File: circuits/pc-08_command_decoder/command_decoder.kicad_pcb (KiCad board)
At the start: 2 copper layers, 99.1 x 99.1 mm, 17 parts, among them U1 74HC138, U2 74HC138, U3 74HC138, U4 74HC138, U5 4011, U6 4011, U7 74HC138, U8 4011

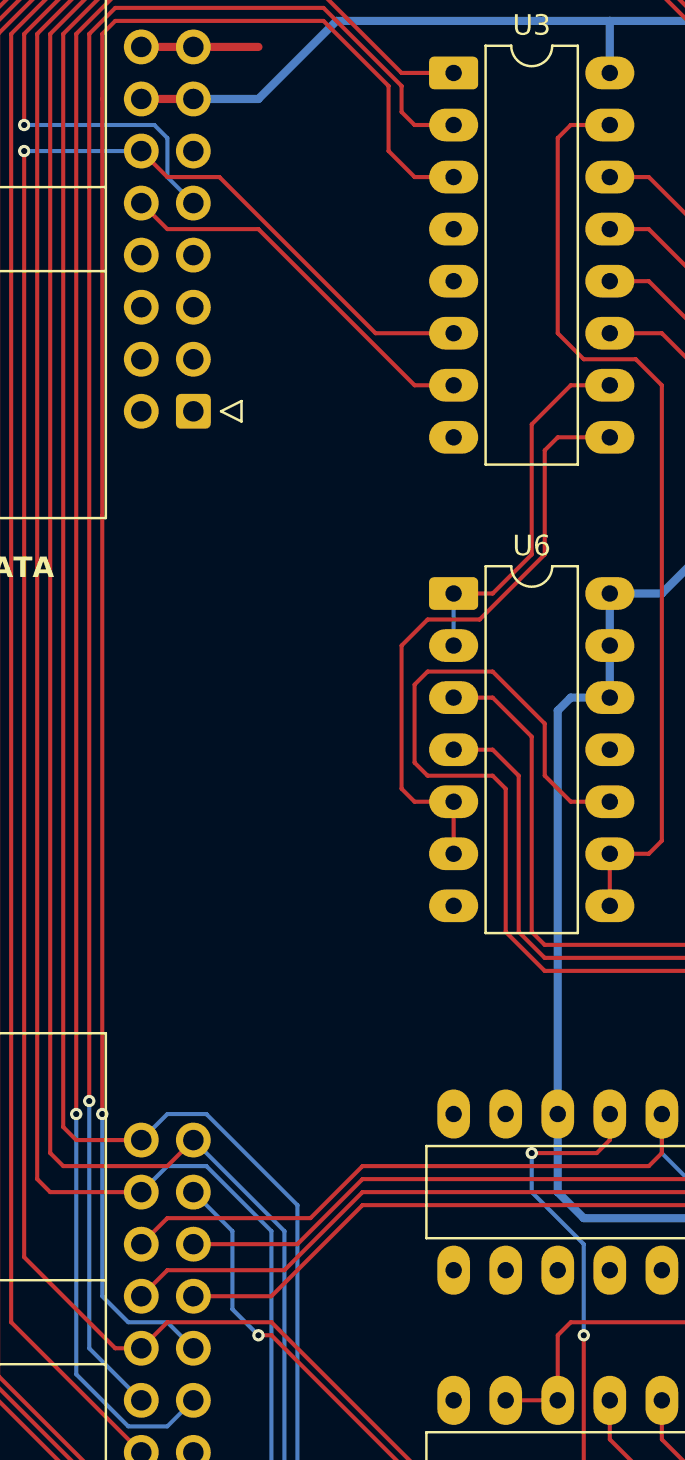
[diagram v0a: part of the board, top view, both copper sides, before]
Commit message: add pull-up resistor network to command decoder
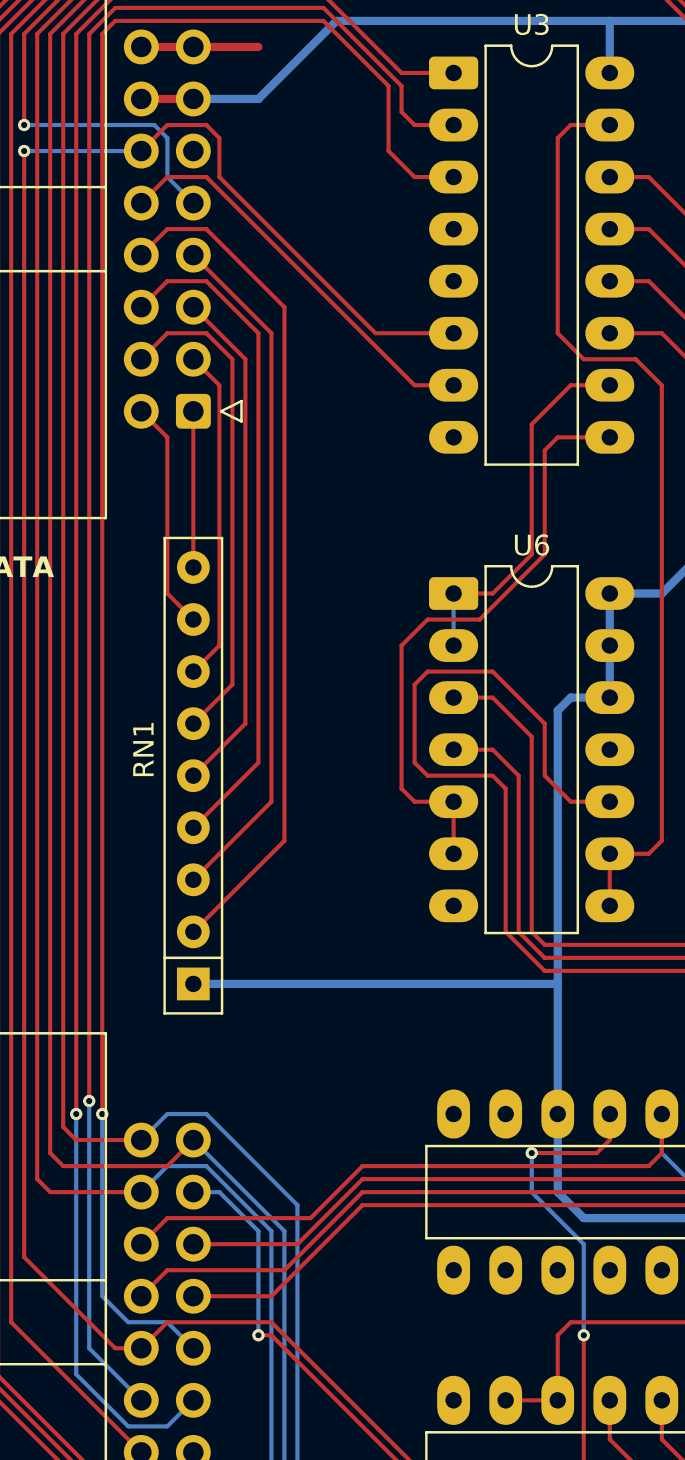
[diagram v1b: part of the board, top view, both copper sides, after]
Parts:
- added RN1: R_Network08, Resistor_THT:R_Array_SIP9, F.Cu at (54.6, 82.5)
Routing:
- net /data7: track 0.00 -> 41.4 mm
- net /data6: track 0.00 -> 33.6 mm
- net /data5: track 0.00 -> 32.7 mm
- net /data4: track 0.00 -> 25.0 mm
- net /data3: track 0.00 -> 24.1 mm
- net VCC: track 233.1 -> 250.9 mm
- net /data2: track 0.00 -> 16.3 mm
- net /data1: track 0.00 -> 11.2 mm
- net /data0: track 0.00 -> 7.62 mm
- net /clock: track 110.3 -> 112.5 mm
- net /~{mem_write}: track 18.9 -> 20.0 mm
- net /action4: track 23.4 -> 24.2 mm

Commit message: pc08: finishing touches and interconnects
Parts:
- added D1: LED, LED_SMD:LED_0603_1608Metric, F.Cu at (114.9, 28.7)
- added J1: Screw_Terminal_01x02, TerminalBlock_TE-Connectivity:TerminalBlock_TE_282834-2_1x02_P2.54mm_Horizontal, F.Cu at (122.6, 27.9)
- added J2: Conn_01x06, Connector_PinHeader_2.54mm:PinHeader_1x06_P2.54mm_Vertical, F.Cu at (62.2, 109.2)
- added J3: Conn_01x03, Connector_PinHeader_2.54mm:PinHeader_1x03_P2.54mm_Vertical, F.Cu at (114.3, 66.0)
- added J4: Conn_01x08, Connector_PinHeader_2.54mm:PinHeader_1x08_P2.54mm_Vertical, B.Cu at (61.0, 62.2)
- added J5: Conn_01x05, Connector_PinHeader_2.54mm:PinHeader_1x05_P2.54mm_Vertical, B.Cu at (101.0, 72.4)
- added J6: Conn_01x07, Connector_PinHeader_2.54mm:PinHeader_1x07_P2.54mm_Vertical, B.Cu at (61.6, 37.5)
- added R1: 1K, Resistor_SMD:R_0603_1608Metric, F.Cu at (114.9, 32.6)
- added RN2: R_Network08, Resistor_THT:R_Array_SIP9, F.Cu at (62.2, 83.8)
- added RN3: R_Network08, Resistor_THT:R_Array_SIP9, F.Cu at (101.0, 58.4)
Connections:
- U1 pad 7: unconnected-(U1-~{Y7}-Pad7) -> Net-(J3-Pin_1)
- U2 pad 10: unconnected-(U2-~{Y5}-Pad10) -> Net-(J3-Pin_2)
- U2 pad 11: unconnected-(U2-~{Y4}-Pad11) -> Net-(J3-Pin_3)
- U7 pad 10: unconnected-(U7-~{Y5}-Pad10) -> Net-(J2-Pin_4)
- U7 pad 11: unconnected-(U7-~{Y4}-Pad11) -> Net-(J2-Pin_3)
- U7 pad 12: unconnected-(U7-~{Y3}-Pad12) -> Net-(J2-Pin_2)
- U7 pad 13: unconnected-(U7-~{Y2}-Pad13) -> Net-(J2-Pin_1)
- U7 pad 7: unconnected-(U7-~{Y7}-Pad7) -> Net-(J2-Pin_6)
- U7 pad 9: unconnected-(U7-~{Y6}-Pad9) -> Net-(J2-Pin_5)
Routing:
- net /clock: track 112.5 -> 182.1 mm, vias 1 -> 2
- net /dtgt2: track 89.5 -> 157.5 mm, vias 1 -> 2
- net /dtgt1: track 89.1 -> 149.5 mm, vias 1 -> 2
- net /dtgt0: track 93.5 -> 149.7 mm, vias 1 -> 2
- net /dsrc1: track 161.9 -> 209.7 mm, vias 0 -> 1
- net /dsrc0: track 166.3 -> 214.0 mm, vias 0 -> 1
- net /dsrc2: track 163.7 -> 211.0 mm, vias 0 -> 1
- net /dsrc3: track 163.7 -> 203.7 mm, vias 0 -> 1
- net VCC: track 250.9 -> 281.0 mm
- net /action4: track 24.2 -> 53.3 mm
- net /carryFlag: track 0.00 -> 26.2 mm, vias 0 -> 1
- net Net-(J2-Pin_1): track 0.00 -> 25.0 mm
- net Net-(J3-Pin_1): track 0.00 -> 22.5 mm
- net /~{readALU}: track 45.4 -> 67.6 mm
- net Net-(J2-Pin_2): track 0.00 -> 20.3 mm
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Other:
- board text added: "13 12 7"
- board text added: "16BIT CONTROL"
- board text added: "4011 (NAND)"
- board text added: "74138 (3-8 DECODER)"
- board text added: "8BIT CONTROL"
- board text added: "ALU CONTROL"
- board text added: "COMMAND BUS"
- board text added: "DATA INTERLINK"
- board text added: "MAIN INTERLINK"
- board text added: "POWER"
- board text added: "SOURCE INTERLINK"
- board text added: "~{ACTION} 2-7"
- board text added: "~{DSRC}"

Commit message: bus spy, mock orchestrator & cleanup
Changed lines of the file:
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@@
 	)
 	(segment
-		(start 101.6 79.375)
-		(end 100.965 78.74)
-		(width 0.2)
-		(layer "F.Cu")
-		(net 45)
-	)
-	(segment
-		(start 100.33 97.79)
+		(start 101.6 81.915)
 		(end 101.6 96.52)
 		(width 0.2)
@@
 	)
 	(segment
+		(start 100.965 81.28)
+		(end 101.6 81.915)
+		(width 0.2)
+		(layer "F.Cu")
+		(net 45)
+	)
+	(segment
 		(start 101.6 96.52)
-		(end 101.6 79.375)
+		(end 100.33 97.79)
 		(width 0.2)
 		(layer "F.Cu")
@@
 	)
 	(via
-		(at 100.965 78.74)
+		(at 100.965 81.28)
 		(size 0.6)
 		(drill 0.3)
 		(layers "F.Cu" "B.Cu")
-		(net 45)
-	)
-	(segment
-		(start 100.965 78.74)
-		(end 100.965 74.295)
-		(width 0.2)
-		(layer "B.Cu")
 		(net 45)
 	)
@@
 		(width 0.2)
 		(layer "B.Cu")
+		(net 45)
+	)
+	(segment
+		(start 100.965 81.28)
+		(end 100.965 74.295)
+		(width 0.2)
+		(layer "B.Cu")

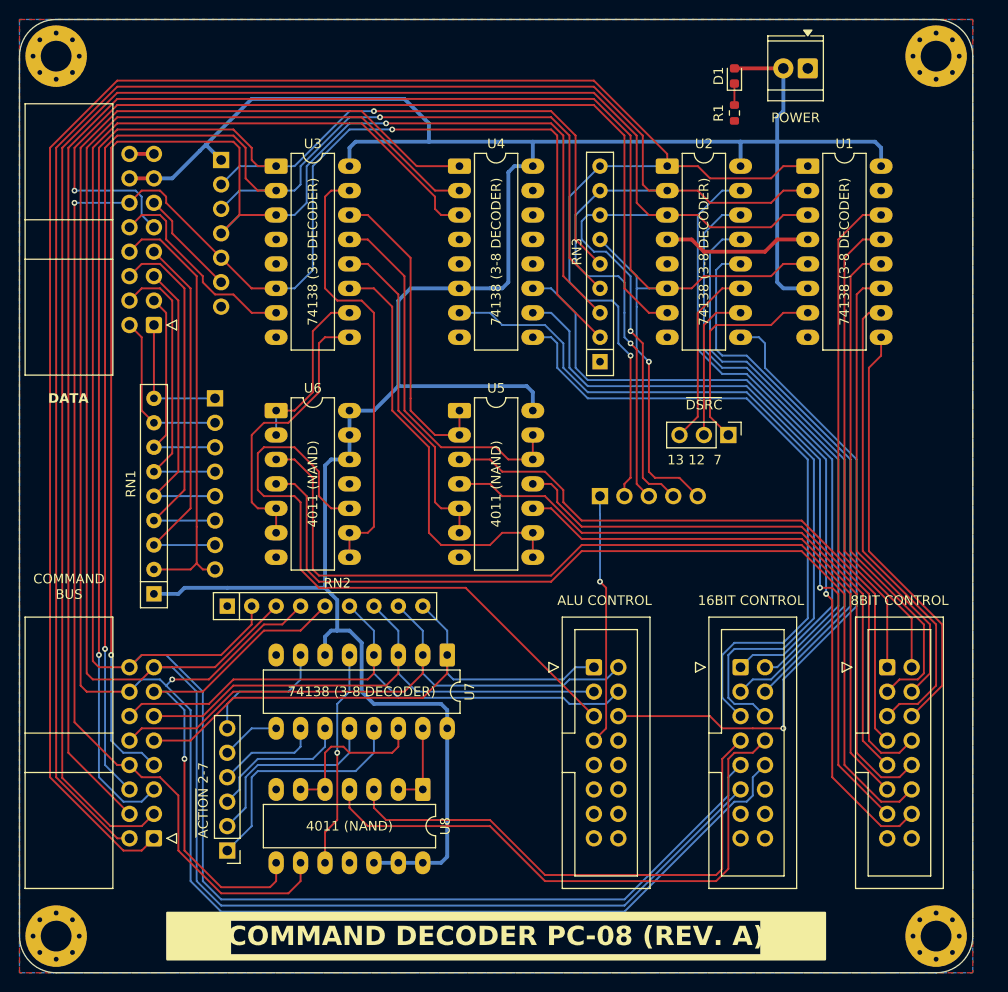
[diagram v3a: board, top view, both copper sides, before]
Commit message: add filter and decoupling capacitors to all boards
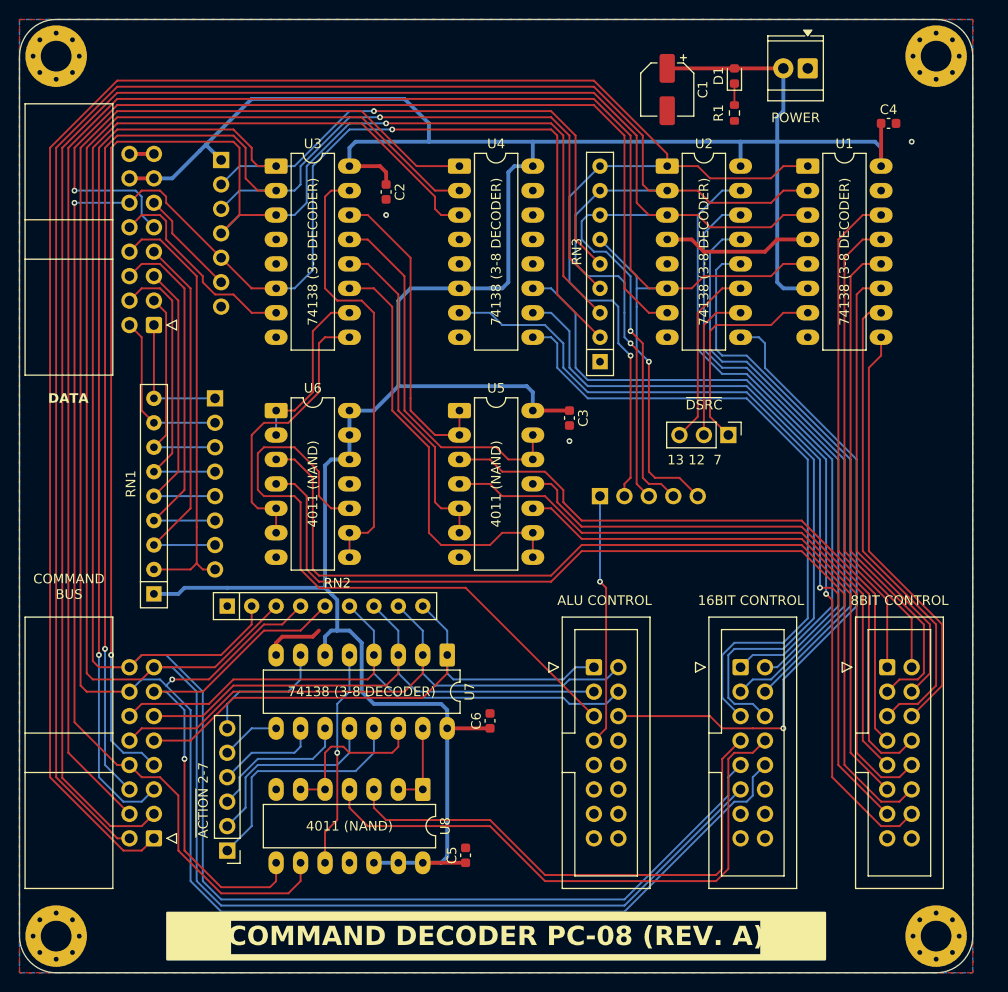
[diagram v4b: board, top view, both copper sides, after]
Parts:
- added C1: C_Polarized, Capacitor_SMD:CP_Elec_5x5.3, F.Cu at (108.0, 30.1)
- added C2: C, Capacitor_SMD:C_0603_1608Metric, F.Cu at (78.7, 40.8)
- added C3: C, Capacitor_SMD:C_0603_1608Metric, F.Cu at (97.8, 64.3)
- added C4: C, Capacitor_SMD:C_0603_1608Metric, F.Cu at (130.9, 33.7)
- added C5: C, Capacitor_SMD:C_0603_1608Metric, F.Cu at (87.0, 109.7)
- added C6: C, Capacitor_SMD:C_0603_1608Metric, F.Cu at (89.5, 95.7)
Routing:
- net VCC: track 281.0 -> 310.5 mm
- net GND: track 18.2 -> 24.4 mm, vias 0 -> 3

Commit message: final touches, pcb ordering
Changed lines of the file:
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@@
 		(min_thickness 0.25)
 		(filled_areas_thickness no)
-		(fill yes
+		(fill
 			(thermal_gap 0.5)
 			(thermal_bridge_width 0.5)
@@
 		(min_thickness 0.25)
 		(filled_areas_thickness no)
-		(fill yes
+		(fill
 			(thermal_gap 0.5)
 			(thermal_bridge_width 0.5)
@@
 		(min_thickness 0.25)
 		(filled_areas_thickness no)
-		(fill yes
+		(fill
 			(thermal_gap 0.5)
 			(thermal_bridge_width 0.5)

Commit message: pc-08 rework
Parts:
- moved CTRL_BUS3 33.0 mm to (133.3, 90.2)
- moved CTRL_BUS1 12.7 mm to (118.1, 90.2)
- moved CTRL_BUS2 12.7 mm to (102.9, 90.2)
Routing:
- net GND: track 24.4 -> 347.3 mm, vias 3 -> 8
- net /action2: track 58.3 -> 103.0 mm, vias 0 -> 1
- net /action3: track 64.4 -> 109.0 mm, vias 0 -> 2
- net /action1: track 65.0 -> 109.1 mm, vias 0 -> 1
- net /writeALU: track 66.5 -> 109.1 mm, vias 0 -> 1
- net /action0: track 59.4 -> 101.4 mm, vias 0 -> 1
- net /carryFlag: track 26.2 -> 55.5 mm, vias 1 -> 2
- net /writePC: track 55.4 -> 34.6 mm
- net /writeSP: track 61.0 -> 41.5 mm
- net /~{readALU}: track 67.6 -> 52.2 mm, vias 1 -> 0
- net /~{readSP_low}: track 62.3 -> 76.8 mm
- net /~{readPC_high}: track 60.9 -> 75.4 mm
- net /~{readSP_high}: track 57.6 -> 71.8 mm
- net /~{readPC_low}: track 65.6 -> 79.4 mm
- net /writeL2: track 97.8 -> 83.9 mm
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
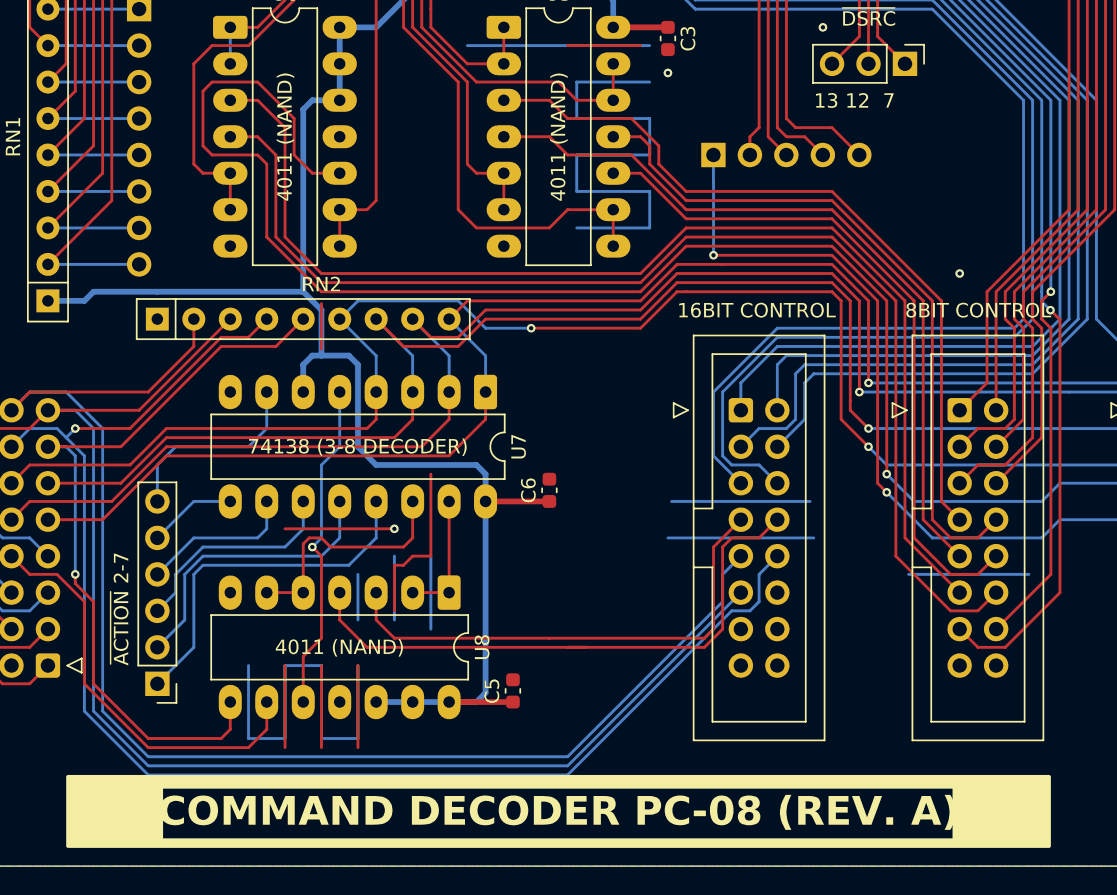
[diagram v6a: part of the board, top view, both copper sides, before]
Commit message: PC-08: fix incorrect dsrc silkscreen
pin labels 12/13 were inverted.
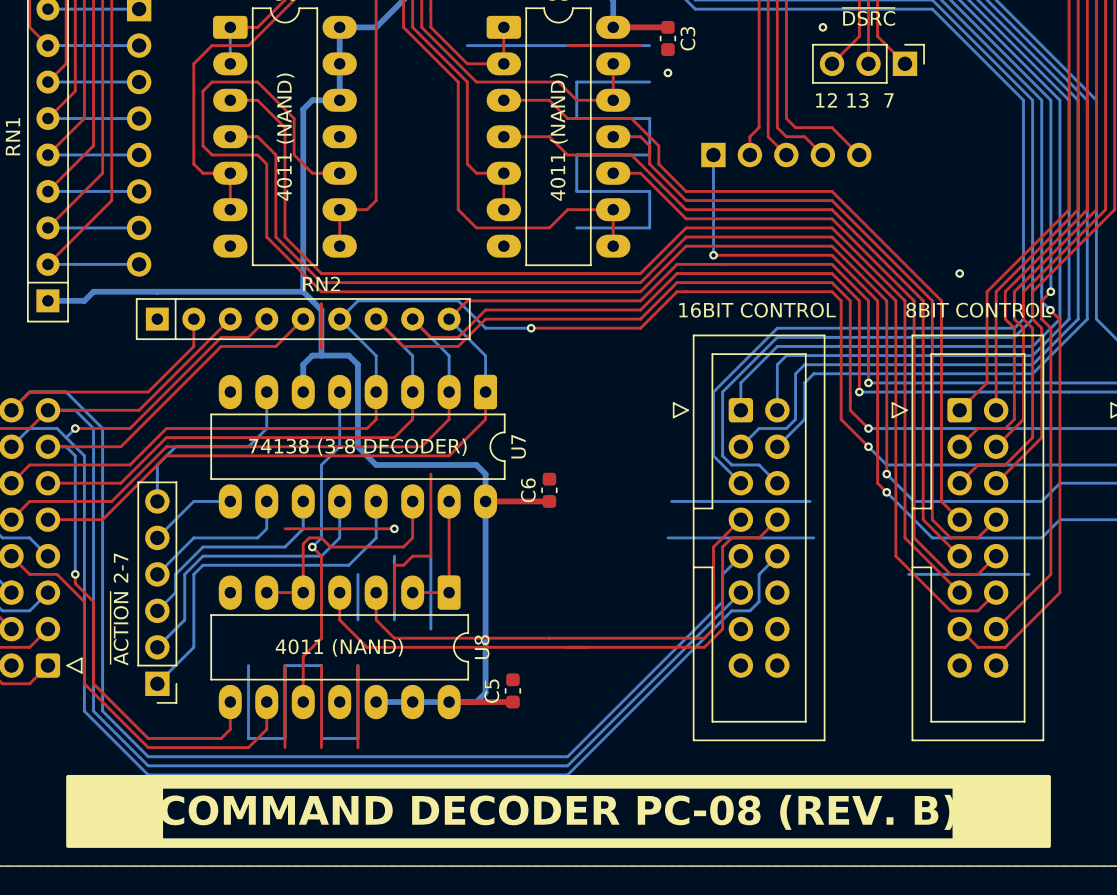
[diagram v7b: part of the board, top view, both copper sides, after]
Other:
- board text added: "12 13 7"
- board text added: "COMMAND DECODER PC-08 (REV. B)"
- board text removed: "13 12 7"
- board text removed: "COMMAND DECODER PC-08 (REV. A)"
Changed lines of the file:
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@@
 		)
 	)
-	(gr_text "13 12  7"
+	(gr_text "12 13  7"
 		(at 107.95 69.215 0)
 		(layer "F.SilkS")
@@
 		)
 	)
-	(gr_text "COMMAND DECODER PC-08 (REV. A)"
+	(gr_text "COMMAND DECODER PC-08 (REV. B)"
 		(at 90.17 118.11 0)
 		(layer "F.SilkS" knockout)
